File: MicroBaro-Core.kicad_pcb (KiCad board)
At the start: 4 copper layers, 26 x 26 mm, 26 parts, among them J1 USB_C_Receptacle_USB2.0_16P, J2 Micro_SD_Card, J3 Conn_01x04, J4 Conn_01x02, U1 ATSAMD20E15A-MUT, U2 BMP390L, U3 BMI160, U4 TPS3839DBZ, U5 TPTLV73333PDBVR

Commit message: Add revision to PCB
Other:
- board text added: "${REVISION}"
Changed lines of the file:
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@@
 		(title "µBaro")
 		(date "2025-03-27")
-		(rev "250327")
+		(rev "v250327")
 		(company "LibreCB")
 	)
@@
 		)
 	)
+	(gr_text "${REVISION}"
+		(at 95.75 81.75 90)
+		(layer "F.SilkS")
+		(effects
+			(font
+				(face "JetBrainsMono NF ExtraBold")
+				(size 1.25 1.25)
+				(thickness 0.3)
+				(bold yes)
+			)
+			(justify left bottom)
+		)
+		(render_cache "v250327" 90
+			(polygon
+				(pts
+					(xy 95.5375 81.387986) (xy 94.575641 81.70802) (xy 94.575641 81.436987) (xy 95.116028 81.26907)
+					(xy 95.217465 81.240219) (xy 95.315391 81.22358) (xy 95.217465 81.207933) (xy 95.117783 81.181677)
+					(xy 94.575641 81.017271) (xy 94.575641 80.742727) (xy 95.5375 81.05925)
+				)
+			)
+			(polygon
+				(pts
+					(xy 95.5375 80.587327) (xy 95.303179 80.587327) (xy 94.82225 80.102887) (xy 94.769613 80.061873)
+					(xy 94.711409 80.037696) (xy 94.645631 80.029461) (xy 94.599459 80.034463) (xy 94.560332 80.048783)
+					(xy 94.526716 80.07228) (xy 94.500671 80.103513) (xy 94.484961 80.140526) (xy 94.47947 80.18509)
+					(xy 94.485135 80.230703) (xy 94.501401 80.268892) (xy 94.528471 80.30141) (xy 94.5634 80.325763)
+					(xy 94.604766 80.340722) (xy 94.654333 80.345985) (xy 94.654333 80.608317) (xy 94.574302 80.601886)
+					(xy 94.503446 80.583346) (xy 94.440162 80.55321) (xy 94.383442 80.511918) (xy 94.335563 80.461519)
+					(xy 94.295906 80.401092) (xy 94.267247 80.334532) (xy 94.249542 80.260111) (xy 94.243394 80.176312)
+					(xy 94.249073 80.094724) (xy 94.26534 80.02298) (xy 94.291479 79.959547) (xy 94.328138 79.901787)
+					(xy 94.372842 79.853705) (xy 94.426195 79.814375) (xy 94.48586 79.785587) (xy 94.552115 79.767956)
+					(xy 94.626397 79.761863) (xy 94.693094 79.766686) (xy 94.758474 79.781163) (xy 94.823165 79.805597)
+					(xy 94.883762 79.839072) (xy 94.946242 79.885637) (xy 95.01108 79.947258) (xy 95.301424 80.25157)
+					(xy 95.301424 79.747895) (xy 95.5375 79.747895)
+				)
+			)
+			(polygon
+				(pts
+					(xy 95.554978 79.1308) (xy 95.548106 79.228653) (xy 95.528697 79.311938) (xy 95.497954 79.383046)
+					(xy 95.456212 79.443889) (xy 95.402821 79.494806) (xy 95.341467 79.530974) (xy 95.270566 79.553253)
+					(xy 95.187774 79.561049) (xy 95.187774 79.298717) (xy 95.228667 79.293346) (xy 95.262166 79.277991)
+					(xy 95.290051 79.252387) (xy 95.310366 79.219554) (xy 95.323125 79.179631) (xy 95.32768 79.1308)
+					(xy 95.322808 79.080963) (xy 95.30941 79.042145) (xy 95.288372 79.011885) (xy 95.259628 78.989083)
+					(xy 95.223861 78.974954) (xy 95.178997 78.969905) (xy 95.089848 78.969905) (xy 95.035294 78.976806)
+					(xy 94.996016 78.995502) (xy 94.967992 79.025329) (xy 94.949788 79.068752) (xy 94.942921 79.1308)
+					(xy 94.942921 79.517315) (xy 94.260873 79.517315) (xy 94.260873 78.754819) (xy 94.496949 78.754819)
+					(xy 94.496949 79.267195) (xy 94.715546 79.267195) (xy 94.715546 79.120344) (xy 94.722541 79.021186)
+					(xy 94.742051 78.93917) (xy 94.772559 78.871298) (xy 94.813548 78.815193) (xy 94.865841 78.769311)
+					(xy 94.927893 78.735998) (xy 95.001663 78.715075) (xy 95.089848 78.70765) (xy 95.178997 78.70765)
+					(xy 95.264887 78.715272) (xy 95.337921 78.736941) (xy 95.400537 78.771832) (xy 95.454457 78.820459)
+					(xy 95.496779 78.87922) (xy 95.528059 78.949008) (xy 95.54791 79.031967)
+				)
+			)
+			(polygon
+				(pts
+					(xy 94.929839 77.959938) (xy 94.95813 77.971136) (xy 94.980549 77.989118) (xy 95.003015 78.026765)
+					(xy 95.01108 78.078266) (xy 95.00311 78.128461) (xy 94.980549 78.166652) (xy 94.958065 78.185127)
+					(xy 94.929772 78.196586) (xy 94.89392 78.200693) (xy 94.858167 78.196546) (xy 94.830545 78.185066)
+					(xy 94.809122 78.166652) (xy 94.787848 78.128597) (xy 94.78027 78.078266) (xy 94.787939 78.026623)
+					(xy 94.809122 77.989118) (xy 94.830478 77.971198) (xy 94.858096 77.959978) (xy 94.89392 77.955916)
+				)
+			)
+			(polygon
+				(pts
+					(xy 95.245778 77.664654) (xy 95.312618 77.682019) (xy 95.372254 77.710223) (xy 95.425468 77.749053)
+					(xy 95.470155 77.797077) (xy 95.506893 77.855318) (xy 95.532904 77.919389) (xy 95.549234 77.993111)
+					(xy 95.554978 78.078266) (xy 95.549273 78.162284) (xy 95.53298 78.23578) (xy 95.506893 78.300375)
+					(xy 95.470108 78.359156) (xy 95.425415 78.407469) (xy 95.372254 78.446386) (xy 95.312618 78.47459)
+					(xy 95.245778 78.491955) (xy 95.170219 78.497982) (xy 94.628153 78.497982) (xy 94.552646 78.491957)
+					(xy 94.485829 78.474592) (xy 94.426195 78.446386) (xy 94.372985 78.407464) (xy 94.328269 78.35915)
+					(xy 94.291479 78.300375) (xy 94.265392 78.23578) (xy 94.249099 78.162284) (xy 94.243394 78.078266)
+					(xy 94.470769 78.078266) (xy 94.475936 78.131538) (xy 94.49022 78.173591) (xy 94.512748 78.206875)
+					(xy 94.543436 78.232164) (xy 94.581199 78.247691) (xy 94.628153 78.253205) (xy 95.170219 78.253205)
+					(xy 95.217104 78.247602) (xy 95.254896 78.231794) (xy 95.2857 78.205959) (xy 95.308333 78.172191)
+					(xy 95.32257 78.130358) (xy 95.32768 78.078266) (xy 95.322513 78.025048) (xy 95.308228 77.983045)
+					(xy 95.2857 77.94981) (xy 95.25496 77.924473) (xy 95.217169 77.908923) (xy 95.170219 77.903404)
+					(xy 94.628153 77.903404) (xy 94.581205 77.908925) (xy 94.543442 77.924476) (xy 94.512748 77.94981)
+					(xy 94.49022 77.983045) (xy 94.475936 78.025048) (xy 94.470769 78.078266) (xy 94.243394 78.078266)
+					(xy 94.249139 77.993111) (xy 94.265468 77.919389) (xy 94.291479 77.855318) (xy 94.328222 77.797082)
+					(xy 94.372932 77.749057) (xy 94.426195 77.710223) (xy 94.485829 77.682016) (xy 94.552646 77.664652)
+					(xy 94.628153 77.658627) (xy 95.170219 77.658627)
+				)
+			)
+			(polygon
+				(pts
+					(xy 95.554978 77.036265) (xy 95.54808 77.134168) (xy 95.528636 77.217122) (xy 95.497894 77.287605)
+					(xy 95.456212 77.347599) (xy 95.402931 77.39767) (xy 95.341618 77.433312) (xy 95.270678 77.455301)
+					(xy 95.187774 77.463003) (xy 95.187774 77.200671) (xy 95.228802 77.195466) (xy 95.262299 77.180645)
+					(xy 95.290051 77.156097) (xy 95.3103 77.124352) (xy 95.323086 77.085074) (xy 95.32768 77.036265)
+					(xy 95.323029 76.986273) (xy 95.310195 76.946803) (xy 95.290051 76.915594) (xy 95.262363 76.891548)
+					(xy 95.228866 76.876983) (xy 95.187774 76.871859) (xy 95.086337 76.871859) (xy 95.040364 76.877046)
+					(xy 95.004091 76.891501) (xy 94.975283 76.914754) (xy 94.95424 76.945568) (xy 94.940797 76.985226)
+					(xy 94.935899 77.036265) (xy 94.935899 77.211128) (xy 94.733025 77.211128) (xy 94.488247 76.931317)
+					(xy 94.488247 77.410491) (xy 94.260873 77.410491) (xy 94.260873 76.648072) (xy 94.472524 76.648072)
+					(xy 94.724323 76.929562) (xy 94.742632 76.855659) (xy 94.769051 76.792828) (xy 94.80314 76.739476)
+					(xy 94.844995 76.694402) (xy 94.894448 76.657854) (xy 94.950036 76.631541) (xy 95.01291 76.615272)
+					(xy 95.084582 76.609603) (xy 95.187774 76.609603) (xy 95.270732 76.61726) (xy 95.341691 76.63911)
+					(xy 95.402984 76.674501) (xy 95.456212 76.724169) (xy 95.497793 76.783664) (xy 95.52854 76.854037)
+					(xy 95.548042 76.937369)
+				)
+			)
+			(polygon
+				(pts
+					(xy 95.5375 76.391235) (xy 95.303179 76.391235) (xy 94.82225 75.906795) (xy 94.769613 75.865781)
+					(xy 94.711409 75.841604) (xy 94.645631 75.833369) (xy 94.599459 75.838371) (xy 94.560332 75.85269)
+					(xy 94.526716 75.876188) (xy 94.500671 75.90742) (xy 94.484961 75.944434) (xy 94.47947 75.988998)
+					(xy 94.485135 76.034611) (xy 94.501401 76.0728) (xy 94.528471 76.105318) (xy 94.5634 76.129671)
+					(xy 94.604766 76.14463) (xy 94.654333 76.149893) (xy 94.654333 76.412225) (xy 94.574302 76.405794)
+					(xy 94.503446 76.387254) (xy 94.440162 76.357117) (xy 94.383442 76.315826) (xy 94.335563 76.265427)
+					(xy 94.295906 76.205) (xy 94.267247 76.13844) (xy 94.249542 76.064019) (xy 94.243394 75.98022)
+					(xy 94.249073 75.898632) (xy 94.26534 75.826888) (xy 94.291479 75.763455) (xy 94.328138 75.705695)
+					(xy 94.372842 75.657613) (xy 94.426195 75.618283) (xy 94.48586 75.589495) (xy 94.552115 75.571864)
+					(xy 94.626397 75.565771) (xy 94.693094 75.570594) (xy 94.758474 75.585071) (xy 94.823165 75.609505)
+					(xy 94.883762 75.642979) (xy 94.946242 75.689545) (xy 95.01108 75.751166) (xy 95.301424 76.055478)
+					(xy 95.301424 75.551803) (xy 95.5375 75.551803)
+				)
+			)
+			(polygon
+				(pts
+					(xy 95.5375 75.21803) (xy 94.488247 74.742367) (xy 94.488247 75.093848) (xy 94.698067 75.093848)
+					(xy 94.698067 75.35618) (xy 94.260873 75.35618) (xy 94.260873 74.459045) (xy 94.486492 74.459045)
+					(xy 95.5375 74.931197)
+				)
+			)
+		)
+	)
 	(gr_text "RST"
 		(at 102 60.25 90)
@@
 				(face "JetBrainsMono NF ExtraBold")
 				(size 1.5 1.5)
-				(thickness 0.3)
-				(bold yes)
+				(thickness 0.1875)
 			)
 			(justify left bottom)

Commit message: Add crystal
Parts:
- added C2: 22pF, Capacitor_SMD:C_0402_1005Metric, F.Cu at (108.1, 68.6)
- added C3: 22pF, Capacitor_SMD:C_0402_1005Metric, F.Cu at (109.3, 74.0)
- added Y1: Crystal_GND24, Crystal:Crystal_SMD_3225-4Pin_3.2x2.5mm, F.Cu at (108.5, 71.3)
- U1: value ATSAMD20E15A-MUT -> ATSAMD21E16B-MU
- moved G*** 12.3 mm to (104.5, 59.5)
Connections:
- U1 pad 13: unconnected-(U1-PA10-Pad13) -> /IMU_INT2
- U1 pad 14: /IMU_INT2 -> /BARO_INT
- U1 pad 15: /BARO_INT -> /XI
- U1 pad 16: Net-(D2-A) -> /XO
- U1 pad 7: unconnected-(U1-PA06-Pad7) -> Net-(D2-A)
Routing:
- net Net-(D2-A): track 20.9 -> 43.6 mm
- net /XI: track 0.00 -> 9.39 mm
- net /XO: track 0.00 -> 6.91 mm
- net /CS: track 6.32 -> 7.36 mm
- net /BARO_INT: track 6.29 -> 7.21 mm
- net Net-(U1-PA23): track 17.2 -> 17.9 mm
- net /MISO: track 8.88 -> 9.43 mm
- net /BUF_I2C_SCL: track 11.7 -> 12.0 mm, vias 0 -> 2
- net /IMU_INT2: track 4.50 -> 4.52 mm, vias 2 -> 0

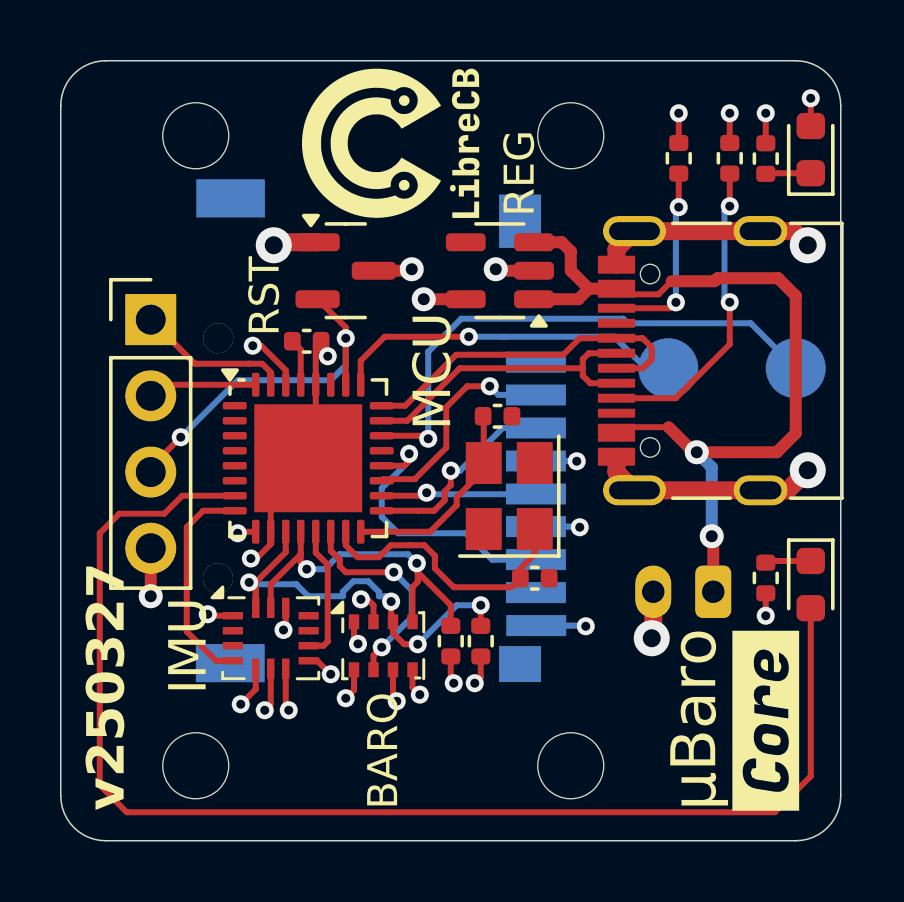
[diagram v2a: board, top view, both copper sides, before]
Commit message: add digikey part numbers
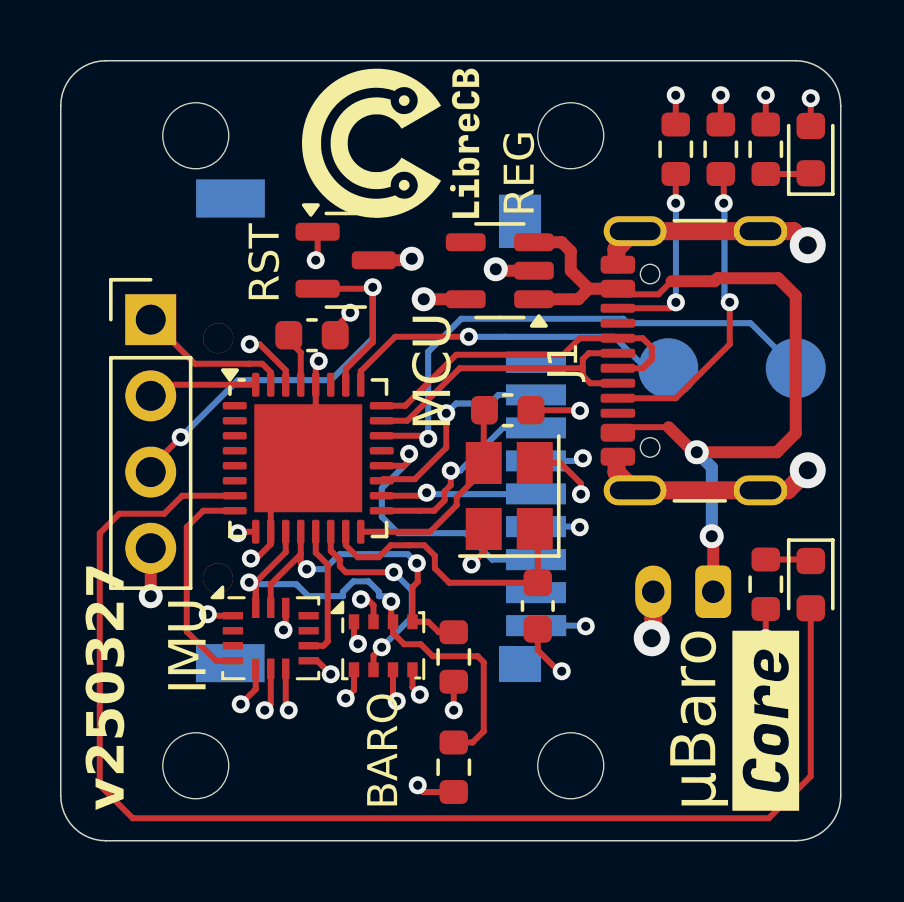
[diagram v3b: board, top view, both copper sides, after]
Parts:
- C1, C2, C3: footprint Capacitor_SMD:C_0402_1005Metric -> Capacitor_SMD:C_0603_1608Metric
- J1: footprint Project:USB_C_Receptacle_G-Switch_GT-USB-7010ASV -> Connector_USB:USB_C_Receptacle_GCT_USB4105-xx-A_16P_TopMnt_Horizontal
- R1, R2, R3, R4, R5, R6: footprint Resistor_SMD:R_0402_1005Metric -> Resistor_SMD:R_0603_1608Metric
- U2: value BMP390L -> BMP390
- Y1: value Crystal_GND24 -> 12MHz
- moved R3 4.30 mm to (106.6, 80.3)
- moved C3 0.93 mm to (109.4, 74.9), turned to -90 degrees
- moved R4 0.54 mm to (106.6, 76.6)
- moved R1 0.42 mm to (115.5, 59.7)
- moved C2 0.39 mm to (108.4, 68.4)
- moved U4 0.35 mm to (103.0, 63.4)
- moved R2 0.32 mm to (114.0, 59.7)
- moved R5 0.31 mm to (117.0, 59.7)
- moved C1 0.27 mm to (101.9, 65.9)
- moved R6 0.21 mm to (117.0, 74.2)
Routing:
- net GND: track 43.5 -> 50.7 mm, vias 21 -> 26
- net Net-(J3-Pin_3): track 12.2 -> 16.5 mm
- net /BUF_I2C_SDA: track 14.8 -> 17.4 mm, vias 4 -> 2
- net /BUF_I2C_SCL: track 12.0 -> 11.1 mm

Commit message: Add BMP390 symbols
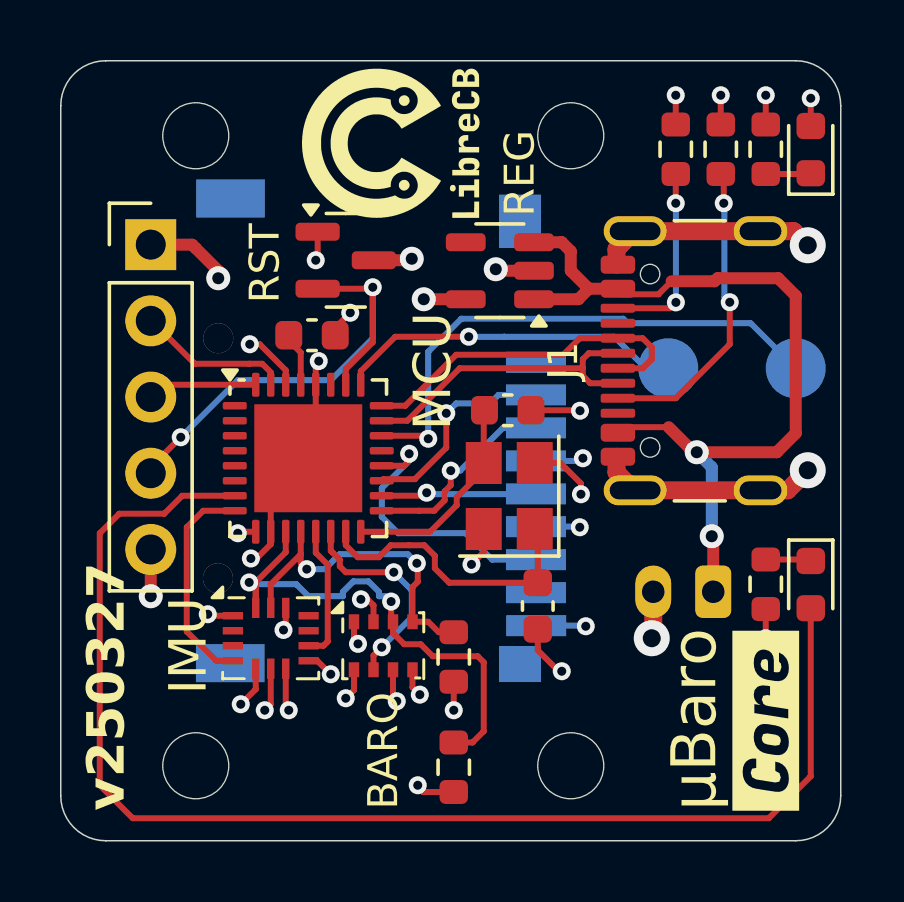
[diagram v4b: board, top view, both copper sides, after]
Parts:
- J3: footprint Connector_PinHeader_2.54mm:PinHeader_1x04_P2.54mm_Vertical -> Connector_PinHeader_2.54mm:PinHeader_1x05_P2.54mm_Vertical
- moved J3 2.50 mm to (96.5, 62.9)
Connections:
- J3 pad 1: Net-(J3-Pin_1) -> +3.3V
- J3 pad 2: Net-(J3-Pin_2) -> /SWCLK
- J3 pad 3: Net-(J3-Pin_3) -> /SWDIO
- J3 pad 4: GND -> Net-(J3-Pin_4)
- U1 pad 26: Net-(J3-Pin_3) -> Net-(J3-Pin_4)
- U1 pad 31: Net-(J3-Pin_1) -> /SWCLK
- U1 pad 32: Net-(J3-Pin_2) -> /SWDIO
- U4 pad 2: Net-(J3-Pin_3) -> Net-(J3-Pin_4)
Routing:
- net Net-(J3-Pin_4): track 0.00 -> 16.5 mm, vias 0 -> 2
- net Net-(J3-Pin_3): track 16.5 -> 0.00 mm, vias 2 -> 0
- net Net-(J3-Pin_1): track 5.14 -> 0.00 mm
- net /SWCLK: track 0.00 -> 5.14 mm
- net Net-(J3-Pin_2): track 3.65 -> 0.00 mm
- net /SWDIO: track 0.00 -> 3.65 mm
- net +3.3V: track 14.1 -> 17.0 mm, vias 12 -> 13
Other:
- board text added: "3.3V"
- board text added: "GND"
- board text added: "NRST"
- board text added: "SWCLK"
- board text added: "SWDIO"

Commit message: Fix wrong footprint on barometer
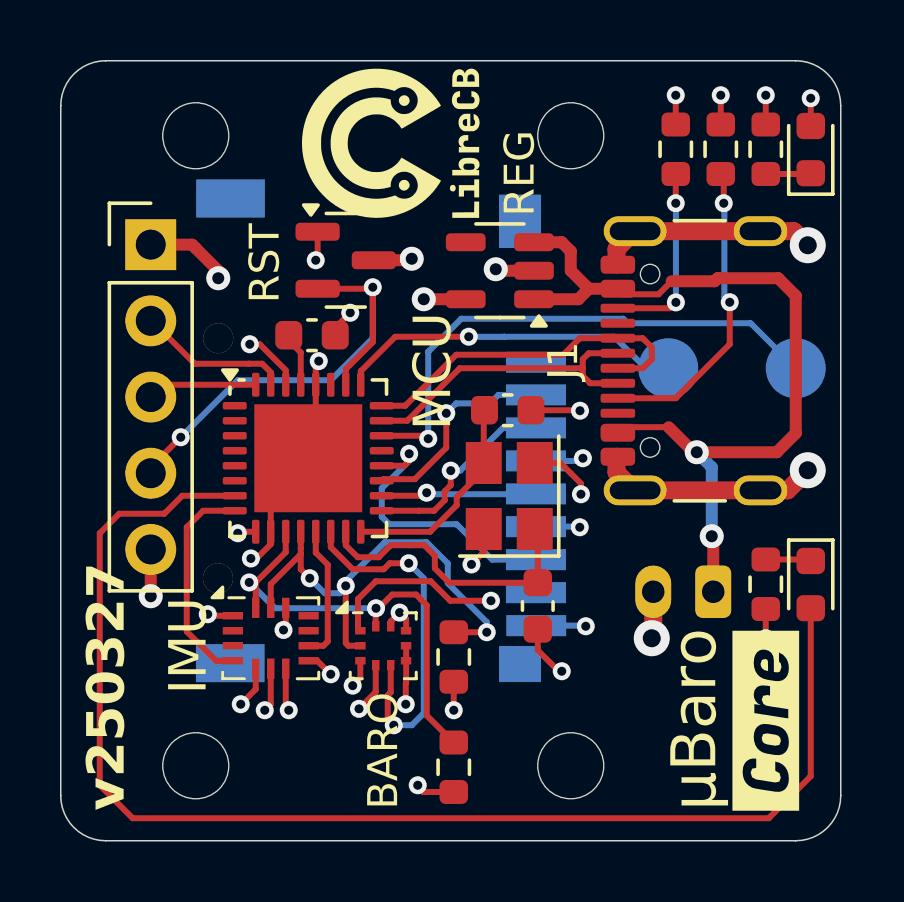
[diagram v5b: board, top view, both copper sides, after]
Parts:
- U2: footprint Package_LGA:Bosch_LGA-8_2x2.5mm_P0.65mm_ClockwisePinNumbering -> Project:Bosch_WFLGA-10_2x2mm_P0.5mm
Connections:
- U2 pad 1: GND -> +3.3V
- U2 pad 2: +3.3V -> /BUF_I2C_SDA
- U2 pad 3: /BUF_I2C_SDA -> GND
- U2 pad 8: +3.3V -> GND
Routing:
- net GND: track 50.7 -> 57.9 mm, vias 26 -> 27
- net /BUF_I2C_SCL: track 11.1 -> 16.2 mm, vias 2 -> 3
- net /BARO_INT: track 7.21 -> 12.0 mm
- net /BUF_I2C_SDA: track 17.4 -> 15.3 mm
- net +3.3V: track 17.0 -> 16.7 mm, vias 13 -> 12
